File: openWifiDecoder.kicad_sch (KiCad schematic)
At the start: 68 parts, among them IC1 DRV8212DRLR, J1 Motor, J24 Hall, U1 MIC5317-1.8xM5, U2 TPS63051RMWR, U3 ESP32-S3-MINI-1, U4 ICM-20948, U5 LTC4054ES5-4.2, U6 TL331, U7 BQ27441DRZT-G1A

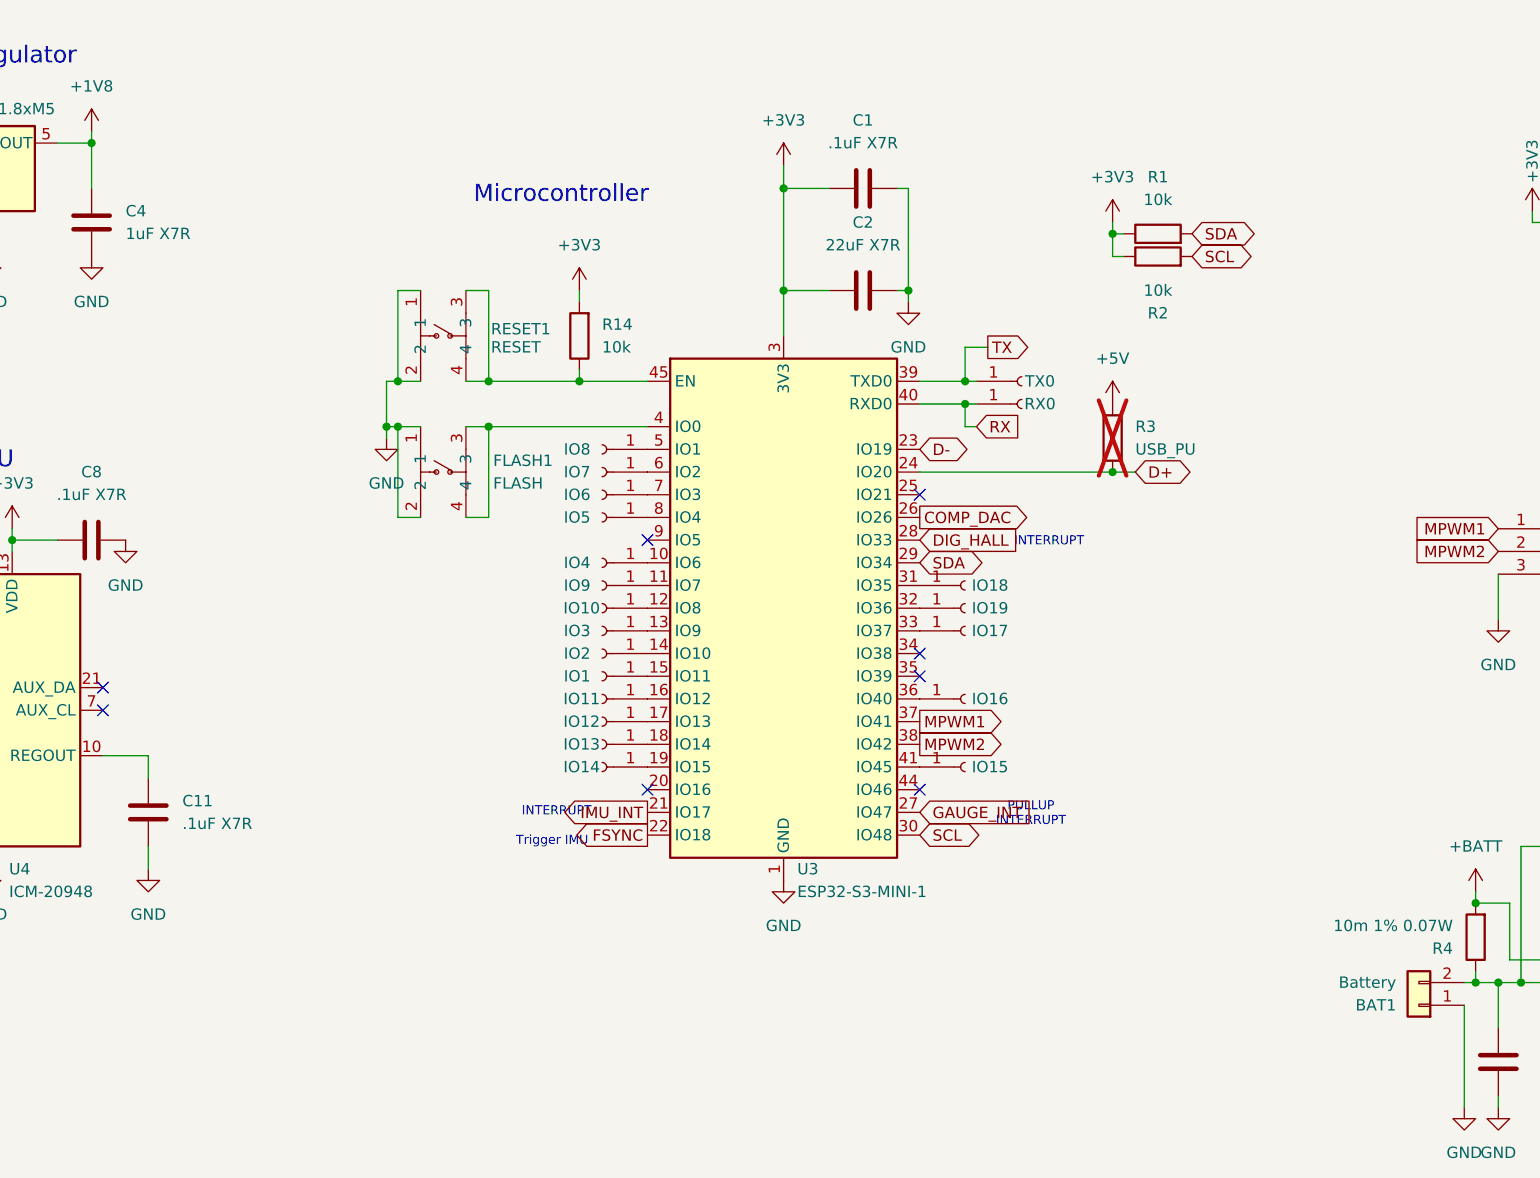
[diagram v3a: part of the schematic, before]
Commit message: add ESP32 chip + flash antenna missing
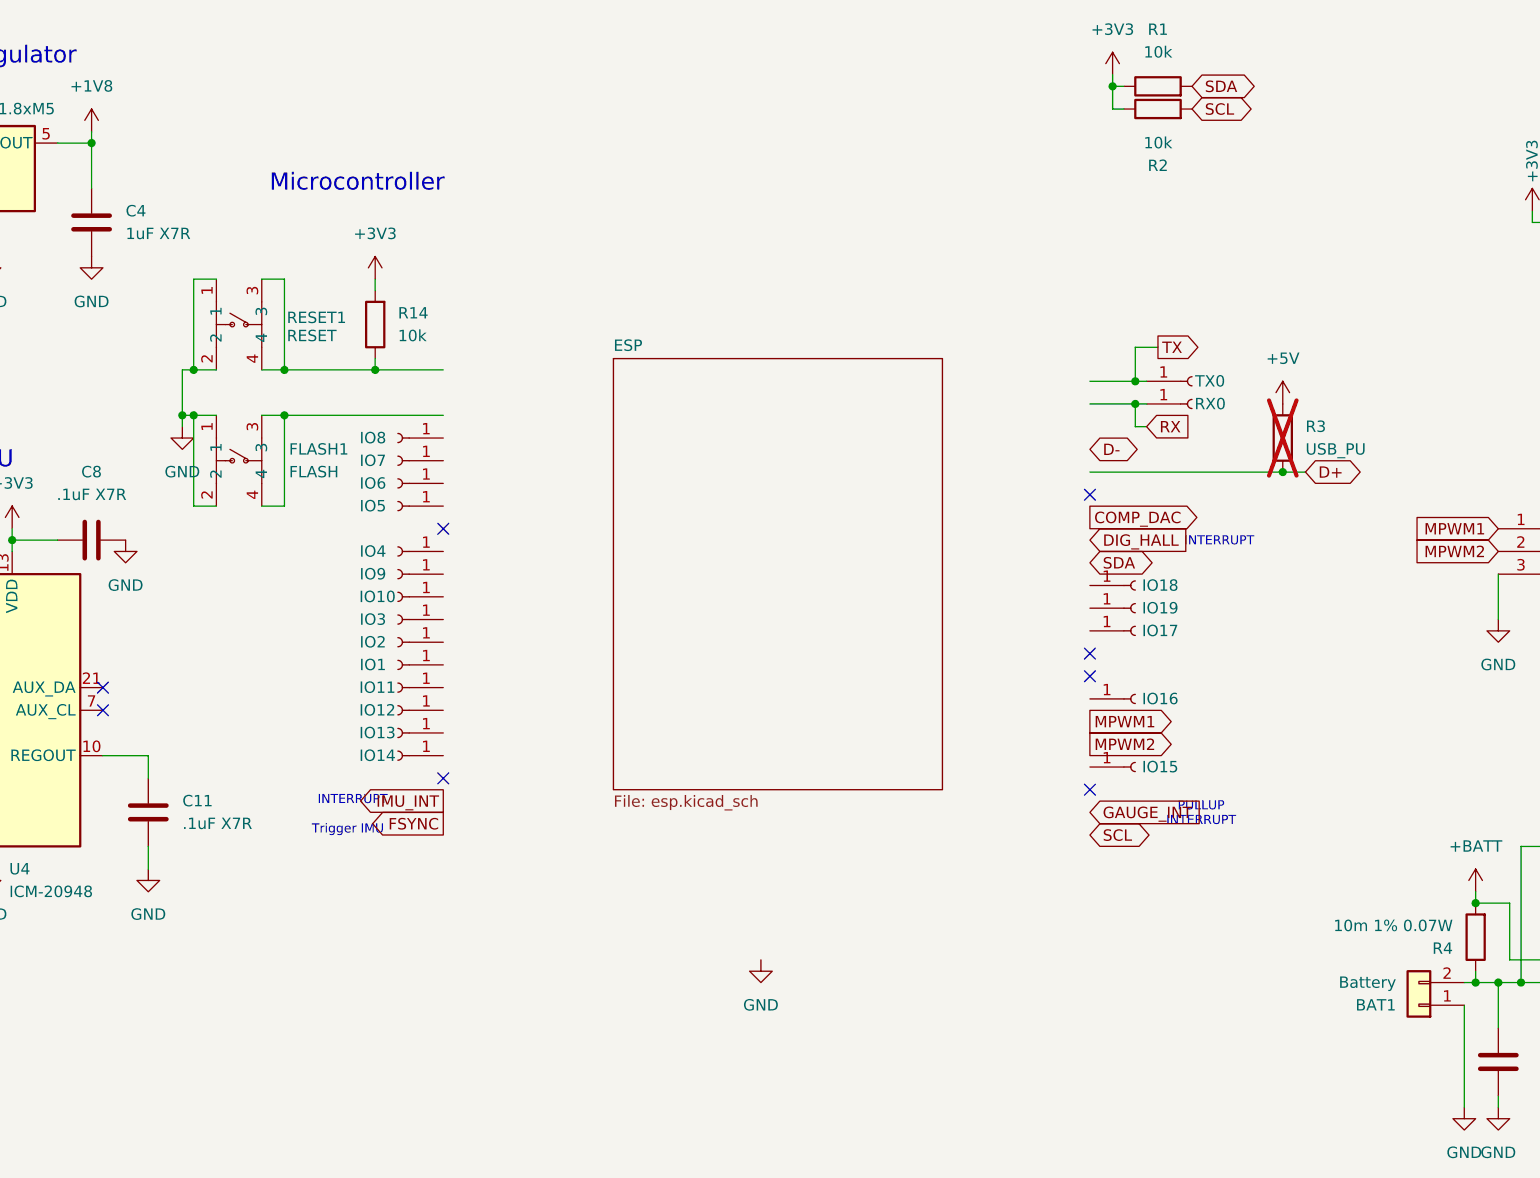
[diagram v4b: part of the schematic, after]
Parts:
- removed C1: .1uF X7R, Capacitor_SMD:C_0402_1005Metric, symbol Device:C
- removed C2: 22uF X7R, Capacitor_SMD:C_0805_2012Metric, symbol Device:C
- removed U3: ESP32-S3-MINI-1, RF_Module:ESP32-S2-MINI-1, symbol RF_Module:ESP32-S3-MINI-1
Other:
- added sheet ESP (esp.kicad_sch)
- moved on the sheet: FLASH1, IO1, IO10, IO11, IO12, IO13, IO14, IO15, IO16, IO17, IO18, IO19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

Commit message: finished Layout, started PCB design agound ESP32
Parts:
- U2: footprint EasyEDA:QFN-12_L2.5-W2.5-P0.50-TL -> EasyEda:QFN-12_L2.5-W2.5-P0.50-TL
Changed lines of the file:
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@@
 			)
 		)
-		(property "Footprint" "EasyEDA:QFN-12_L2.5-W2.5-P0.50-TL"
+		(property "Footprint" "EasyEda:QFN-12_L2.5-W2.5-P0.50-TL"
 			(at 251.46 46.99 0)
 			(effects

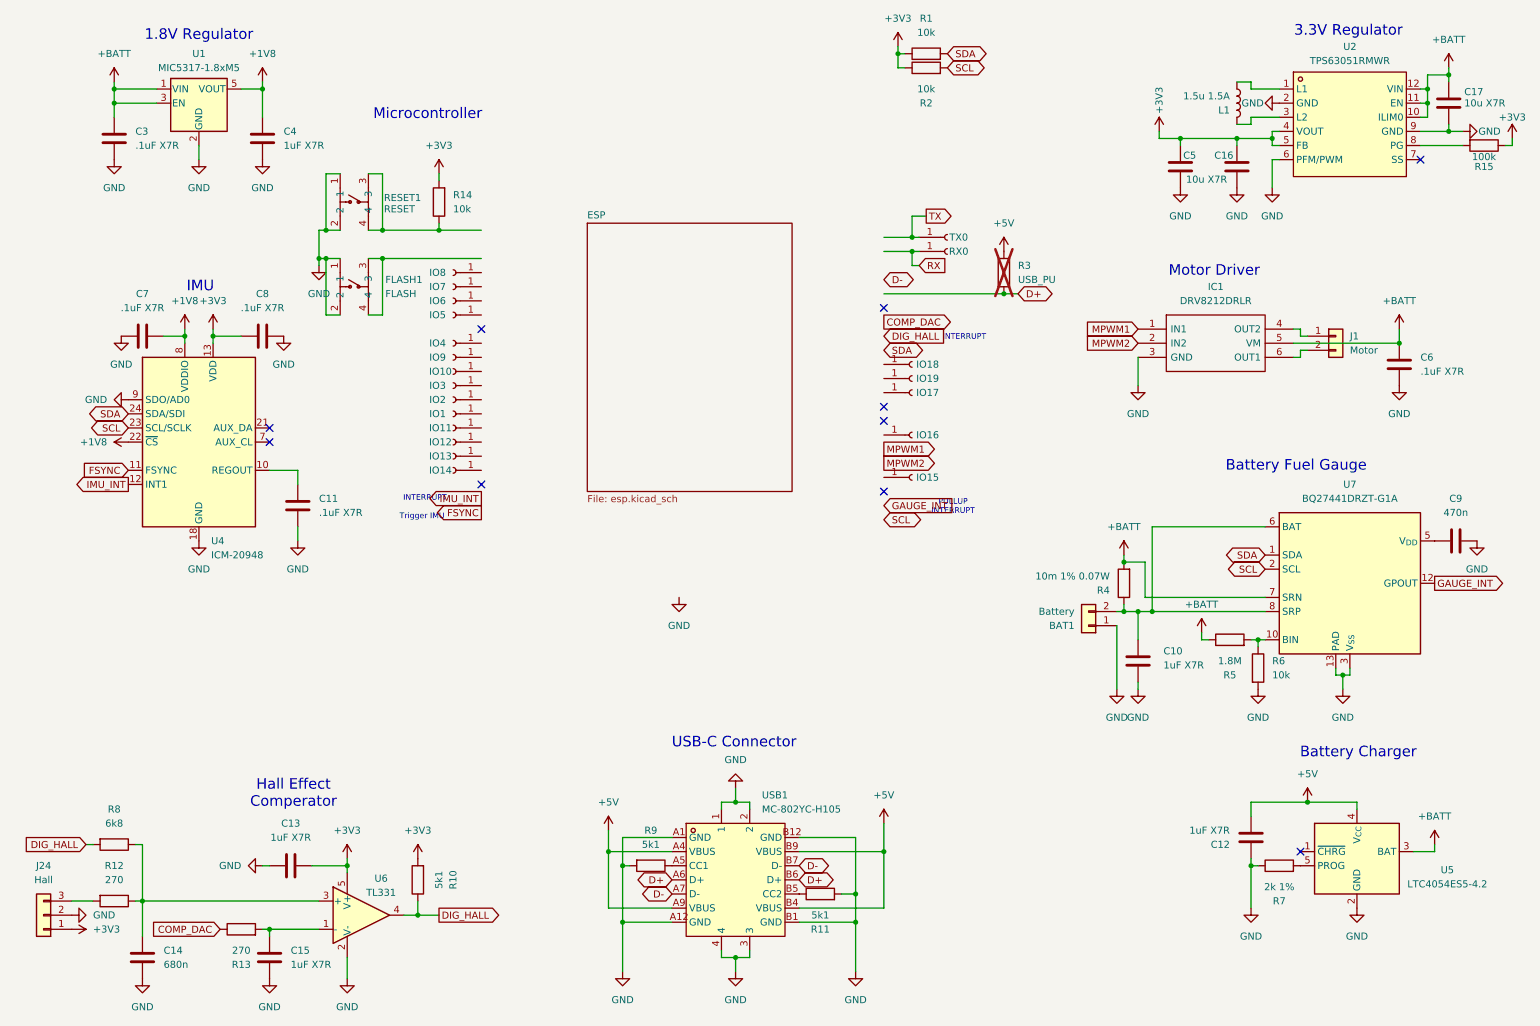
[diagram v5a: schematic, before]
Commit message: pcb parts placed not connected
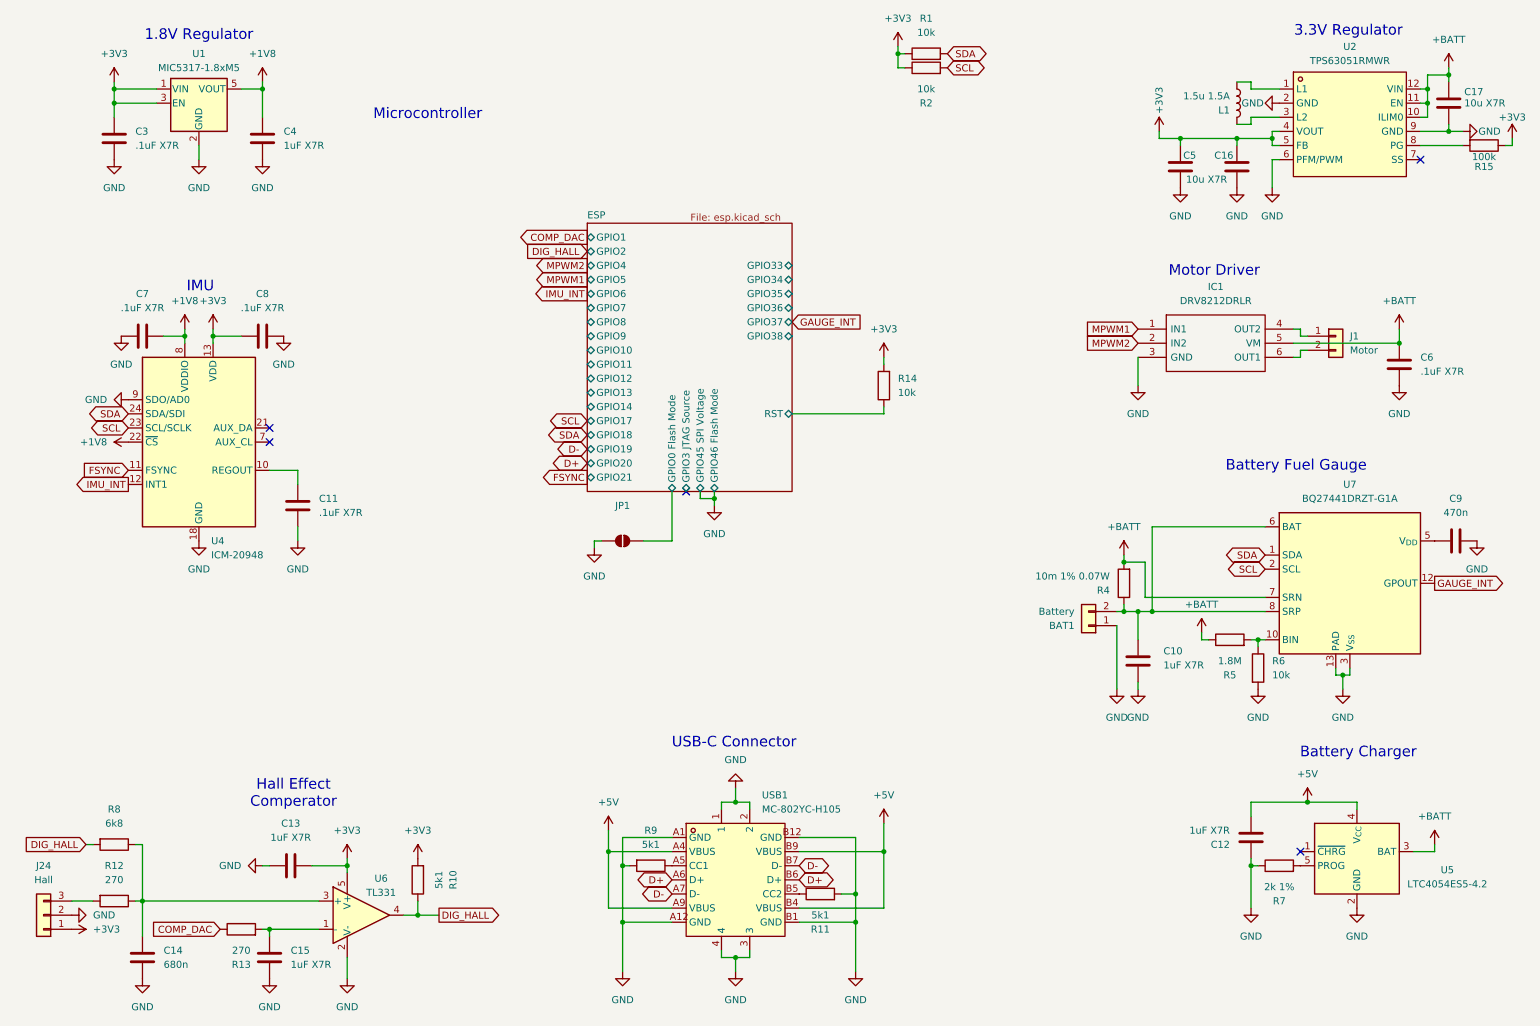
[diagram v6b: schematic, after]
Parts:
- removed FLASH1: FLASH, easyeda2kicad:SW-SMD_4P-L2.6-W1.6-P0.75-LS3.0, symbol easyeda2kicad:1TS026A-1600-0553-CT
- removed IO1, IO8: 1, padLib:SolderPad_1mm_1Pin, symbol Connector:Conn_01x01_Socket
- removed IO10, IO11, IO12, IO13, IO14, IO15, IO16, IO17, IO18, IO19, IO4, IO5, IO6, IO9, RX0, TX0: Conn_01x01_Socket, padLib:SolderPad_1mm_1Pin, symbol Connector:Conn_01x01_Socket
- removed IO2, IO7: 2, padLib:SolderPad_1mm_1Pin, symbol Connector:Conn_01x01_Socket
- removed IO3: 3, padLib:SolderPad_1mm_1Pin, symbol Connector:Conn_01x01_Socket
- removed R3: USB_PU, Resistor_SMD:R_0402_1005Metric, symbol Device:R
- removed RESET1: RESET, easyeda2kicad:SW-SMD_4P-L2.6-W1.6-P0.75-LS3.0, symbol easyeda2kicad:1TS026A-1600-0553-CT
- added JP1: Download Mode, padLib:SolderJumper-2_P1.3mm_Open_TrianglePad1.0x1.5mm_SMALLER, symbol Jumper:SolderJumper_2_Open
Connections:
- net +3V3: now also C3.1, U1.1 (VIN), U1.3 (EN)
- net +BATT: no longer C3.1, U1.1 (VIN), U1.3 (EN)
- net GND: now also JP1.1 (A)
- net ESP/RST: now reaches R14.1
- new net ESP/GPIO0 Flash Mode: JP1.2 (B)
- no-connect marks 10 -> 5
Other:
- sheet ESP ports: added GPIO0 Flash Mode, GPIO1, GPIO10, GPIO11, GPIO12, GPIO13, GPIO14, GPIO17, GPIO18, GPIO19, GPIO2, GPIO20, GPIO21, GPIO3 JTAG Source, GPIO33, GPIO34, GPIO35, GPIO36, GPIO37, GPIO38, GPIO4, GPIO45 SPI Voltage, GPIO46 Flash Mode, GPIO5, GPIO6, GPIO7, GPIO8, GPIO9, RST; removed none
- note removed: "INTERRUPT"
- note removed: "PULLUP INTERRUPT"
- note removed: "Trigger IMU"
- moved on the sheet: R14

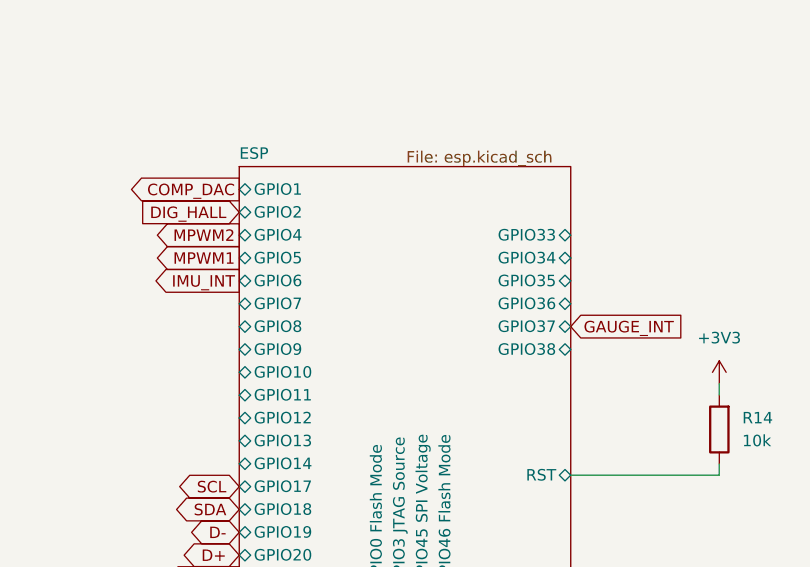
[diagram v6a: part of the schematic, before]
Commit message: pcb complete, drc failing 133 Errors
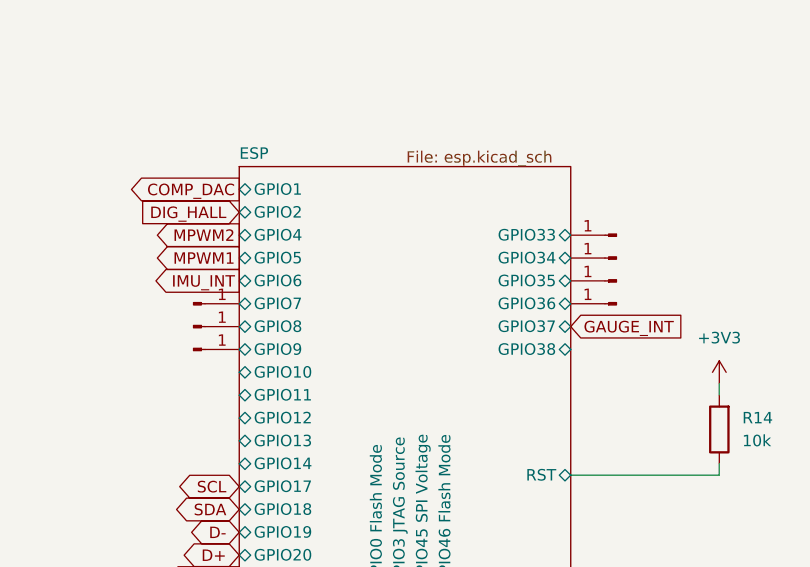
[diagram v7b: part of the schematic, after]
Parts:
- added J2, J3, J4, J5, J6, J7, J8: Conn_01x01_Pin, padLib:SolderPad_1mm_1Pin, symbol Connector:Conn_01x01_Pin
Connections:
- net ESP/GPIO33: now also J5.1 (Pin_1)
- net ESP/GPIO34: now also J6.1 (Pin_1)
- net ESP/GPIO35: now also J7.1 (Pin_1)
- net ESP/GPIO36: now also J8.1 (Pin_1)
- net ESP/GPIO7: now also J2.1 (Pin_1)
- net ESP/GPIO8: now also J3.1 (Pin_1)
- net ESP/GPIO9: now also J4.1 (Pin_1)
